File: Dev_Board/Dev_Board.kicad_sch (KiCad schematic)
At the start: 13 parts

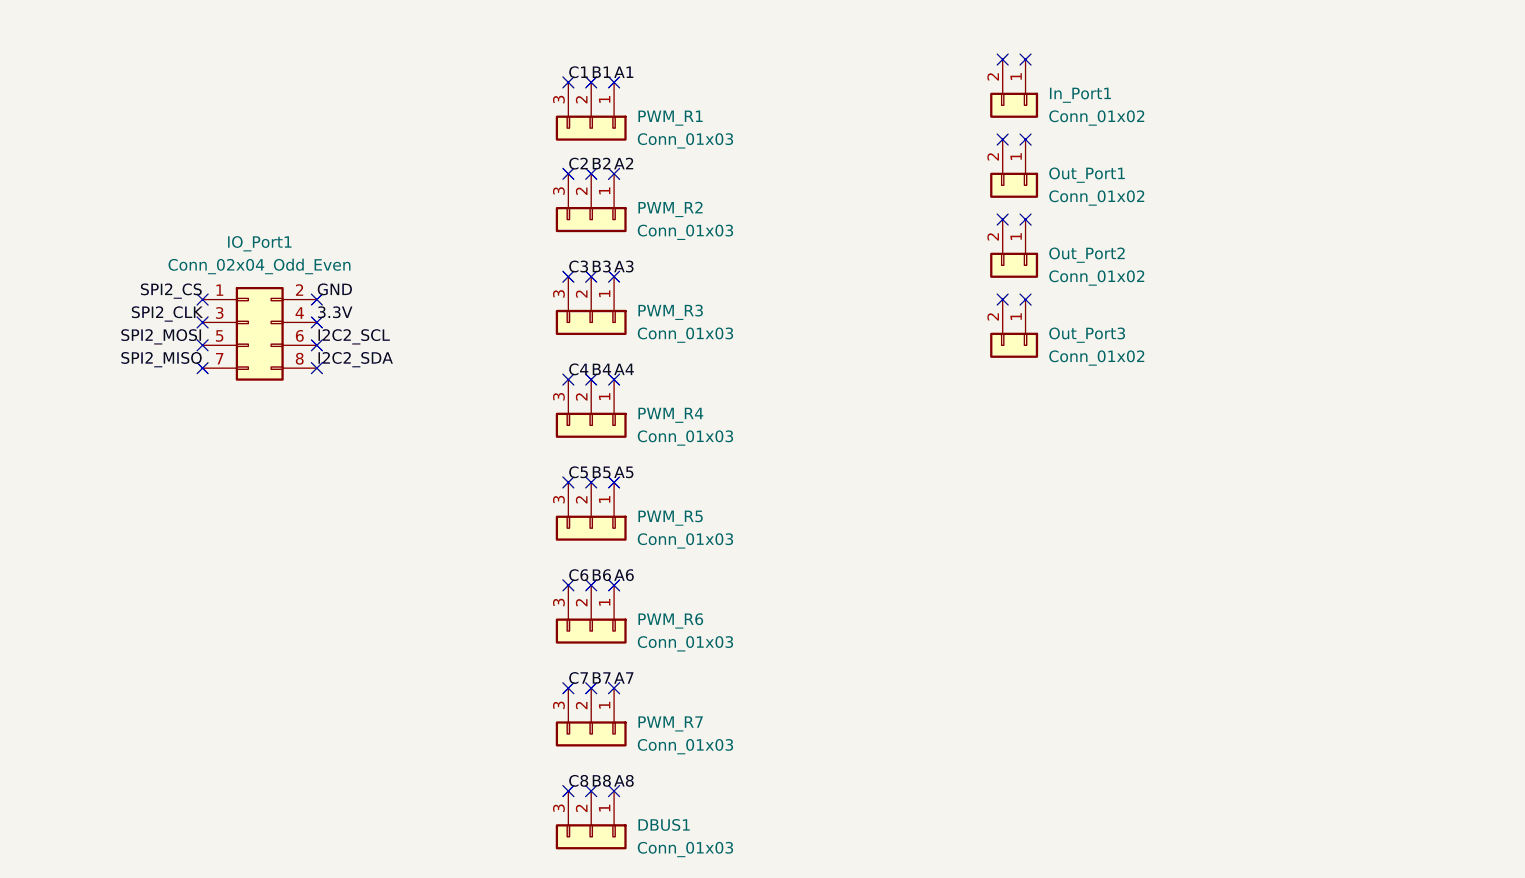
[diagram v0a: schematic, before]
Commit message: added more pins to have different sets on the front and back sides. also changed the courtyards on some footprints because of errors. there are still like 3 courtyard errors
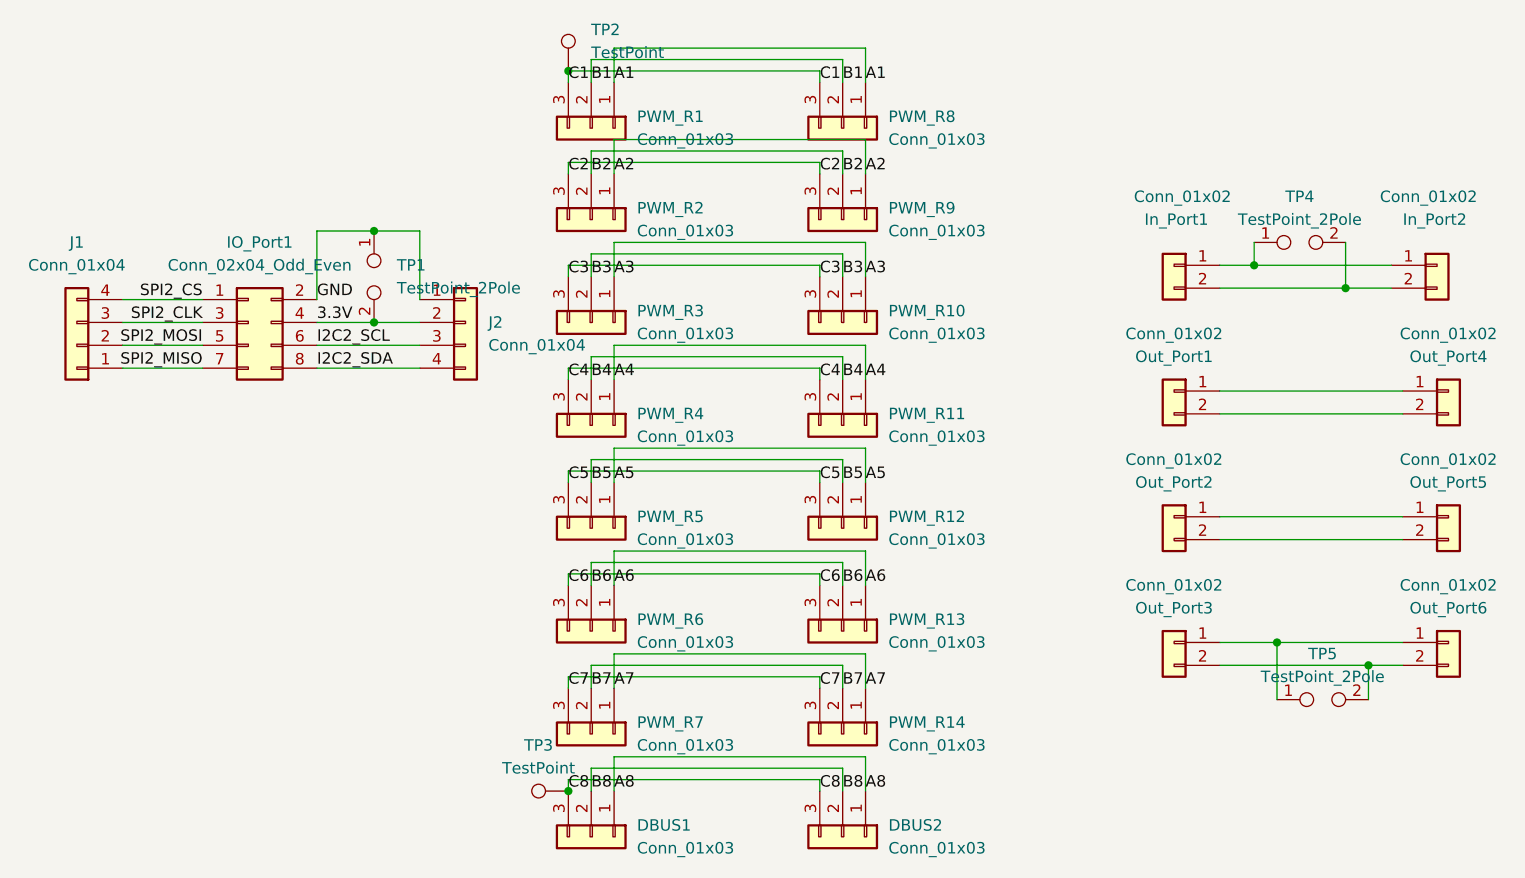
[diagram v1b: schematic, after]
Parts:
- added DBUS2, PWM_R10, PWM_R11, PWM_R12, PWM_R13, PWM_R14, PWM_R8, PWM_R9: Conn_01x03, dev_board_footprints:PinHeader_1x03_2.54mm_Vertical_small_courtyards, symbol Connector_Generic:Conn_01x03
- added In_Port2: Conn_01x02, dev_board_footprints:AMASS_XT30UPB-M_1x02_P5.0mm_Vertical_small_courtyards, symbol Connector_Generic:Conn_01x02
- added J1, J2: Conn_01x04, Connector_PinHeader_2.54mm:PinHeader_1x04_P2.54mm_Vertical, symbol Connector_Generic:Conn_01x04
- added Out_Port4, Out_Port5, Out_Port6: Conn_01x02, dev_board_footprints:AMASS_XT30UPB-F_1x02_P5.0mm_Vertical_small_courtyards, symbol Connector_Generic:Conn_01x02
- added TP1, TP4, TP5: TestPoint_2Pole, TestPoint:TestPoint_2Pads_Pitch2.54mm_Drill0.8mm, symbol Connector:TestPoint_2Pole
- added TP2, TP3: TestPoint, TestPoint:TestPoint_Pad_2.0x2.0mm, symbol Connector:TestPoint
- DBUS1, PWM_R1, PWM_R2, PWM_R3, PWM_R4, PWM_R5, PWM_R6, PWM_R7: footprint Connector_PinHeader_2.54mm:PinHeader_1x03_P2.54mm_Vertical -> dev_board_footprints:PinHeader_1x03_2.54mm_Vertical_small_courtyards
- In_Port1: footprint Connector_AMASS:AMASS_XT30U-M_1x02_P5.0mm_Vertical -> dev_board_footprints:AMASS_XT30UPB-M_1x02_P5.0mm_Vertical_small_courtyards
- Out_Port1, Out_Port2, Out_Port3: footprint Connector_AMASS:AMASS_XT30U-F_1x02_P5.0mm_Vertical -> dev_board_footprints:AMASS_XT30UPB-F_1x02_P5.0mm_Vertical_small_courtyards
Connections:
- net 3.3V: now also J2.2 (Pin_2), TP1.2
- net A1: now also PWM_R8.1 (Pin_1)
- net A2: now also PWM_R9.1 (Pin_1)
- net A3: now also PWM_R10.1 (Pin_1)
- net A4: now also PWM_R11.1 (Pin_1)
- net A5: now also PWM_R12.1 (Pin_1)
- net A6: now also PWM_R13.1 (Pin_1)
- net A7: now also PWM_R14.1 (Pin_1)
- net A8: now also DBUS2.1 (Pin_1)
- net B1: now also PWM_R8.2 (Pin_2)
- net B2: now also PWM_R9.2 (Pin_2)
- net B3: now also PWM_R10.2 (Pin_2)
- net B4: now also PWM_R11.2 (Pin_2)
- net B5: now also PWM_R12.2 (Pin_2)
- net B6: now also PWM_R13.2 (Pin_2)
- net B7: now also PWM_R14.2 (Pin_2)
- net B8: now also DBUS2.2 (Pin_2)
- net C1: now also PWM_R8.3 (Pin_3), TP2.1
- net C2: now also PWM_R9.3 (Pin_3)
- net C3: now also PWM_R10.3 (Pin_3)
- net C4: now also PWM_R11.3 (Pin_3)
- net C5: now also PWM_R12.3 (Pin_3)
- net C6: now also PWM_R13.3 (Pin_3)
- net C7: now also PWM_R14.3 (Pin_3)
- net C8: now also DBUS2.3 (Pin_3), TP3.1
- net GND: now also J2.1 (Pin_1), TP1.1
- net I2C2_SCL: now also J2.3 (Pin_3)
- net I2C2_SDA: now also J2.4 (Pin_4)
- net SPI2_CLK: now also J1.3 (Pin_3)
- net SPI2_CS: now also J1.4 (Pin_4)
- net SPI2_MISO: now also J1.1 (Pin_1)
- net SPI2_MOSI: now also J1.2 (Pin_2)
- net at Out_Port2.1 (Pin_1): now also Out_Port5.1 (Pin_1)
- net at Out_Port2.2 (Pin_2): now also Out_Port5.2 (Pin_2)
- net at In_Port1.1 (Pin_1): now also In_Port2.1 (Pin_1), TP4.1
- net at In_Port1.2 (Pin_2): now also In_Port2.2 (Pin_2), TP4.2
- net at Out_Port3.1 (Pin_1): now also Out_Port6.1 (Pin_1), TP5.1
- net at Out_Port3.2 (Pin_2): now also Out_Port6.2 (Pin_2), TP5.2
- net at Out_Port1.1 (Pin_1): now also Out_Port4.1 (Pin_1)
- net at Out_Port1.2 (Pin_2): now also Out_Port4.2 (Pin_2)
- no-connect marks 40 -> 0
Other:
- moved on the sheet: In_Port1, Out_Port1, Out_Port2, Out_Port3

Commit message: fixed male parts, made tracks wider, made lakshay changes
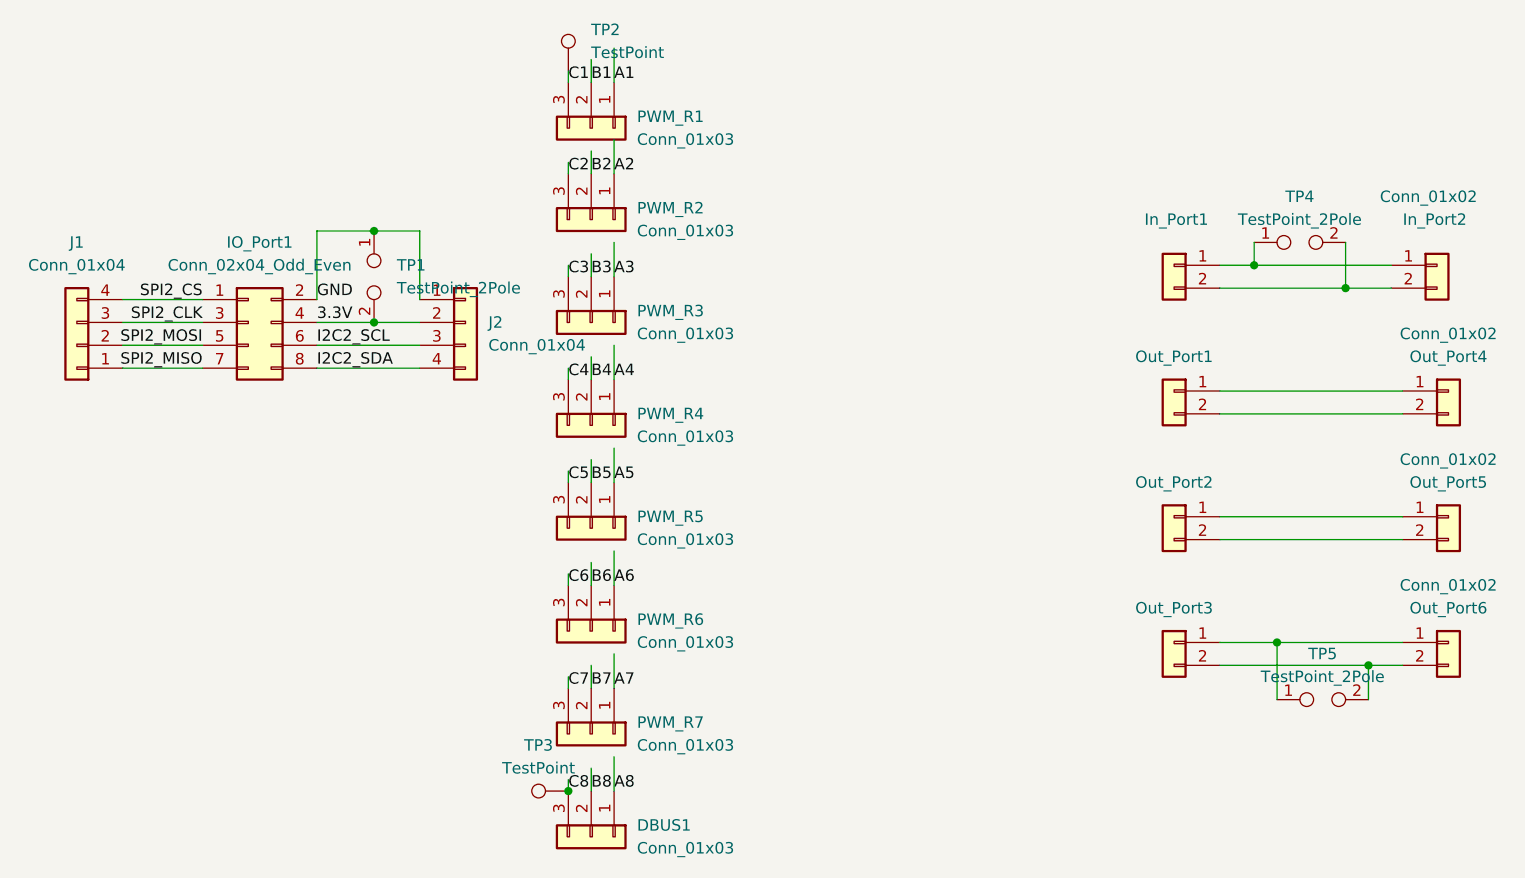
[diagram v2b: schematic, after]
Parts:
- removed DBUS2, PWM_R10, PWM_R11, PWM_R12, PWM_R13, PWM_R14, PWM_R8, PWM_R9: Conn_01x03, dev_board_footprints:PinHeader_1x03_2.54mm_Vertical_small_courtyards, symbol Connector_Generic:Conn_01x03

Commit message: Winter Break Changes
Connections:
- net GND: now also In_Port1.1 (Pin_1), In_Port2.1 (Pin_1), Out_Port1.1 (Pin_1), Out_Port2.1 (Pin_1), Out_Port3.1 (Pin_1), Out_Port4.1 (Pin_1), Out_Port5.1 (Pin_1), Out_Port6.1 (Pin_1), TP4.1, TP5.1
- net +24V: now reaches Out_Port1.2 (Pin_2), Out_Port4.2 (Pin_2)
- net +24V: now also In_Port1.2 (Pin_2), In_Port2.2 (Pin_2), Out_Port2.2 (Pin_2), Out_Port3.2 (Pin_2), Out_Port5.2 (Pin_2), Out_Port6.2 (Pin_2), TP4.2, TP5.2
- net 3.3V renamed +3.3V
- net A1 renamed A1 (GND)
- net A8 renamed A8M (GND)
- net B1 renamed B1 (5V)
- net B8 renamed B8 (5V)
